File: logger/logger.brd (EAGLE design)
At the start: 100 x 80 mm, 18 parts, among them IC1 75176AD, U1 MSP430G2352IPW14

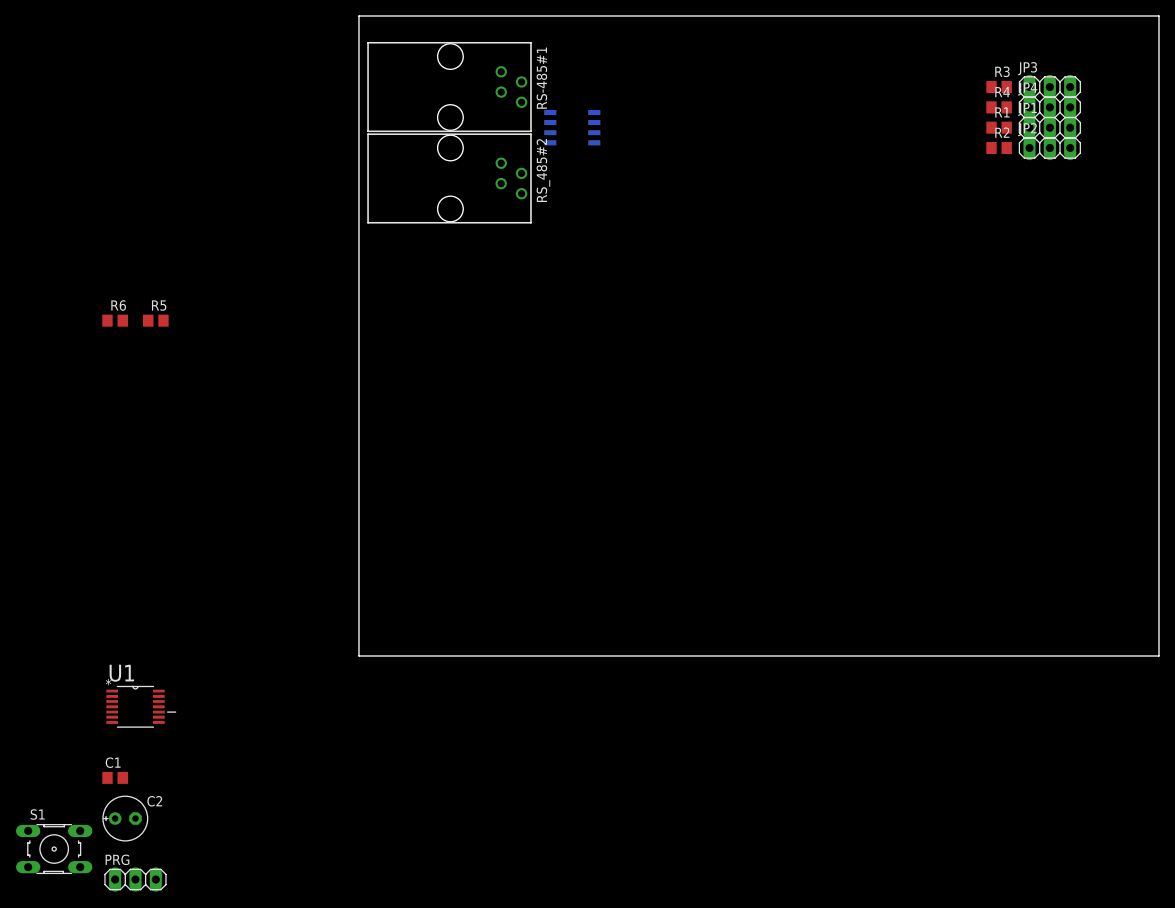
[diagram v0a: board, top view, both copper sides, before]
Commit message: Bugfixes, partially routed.
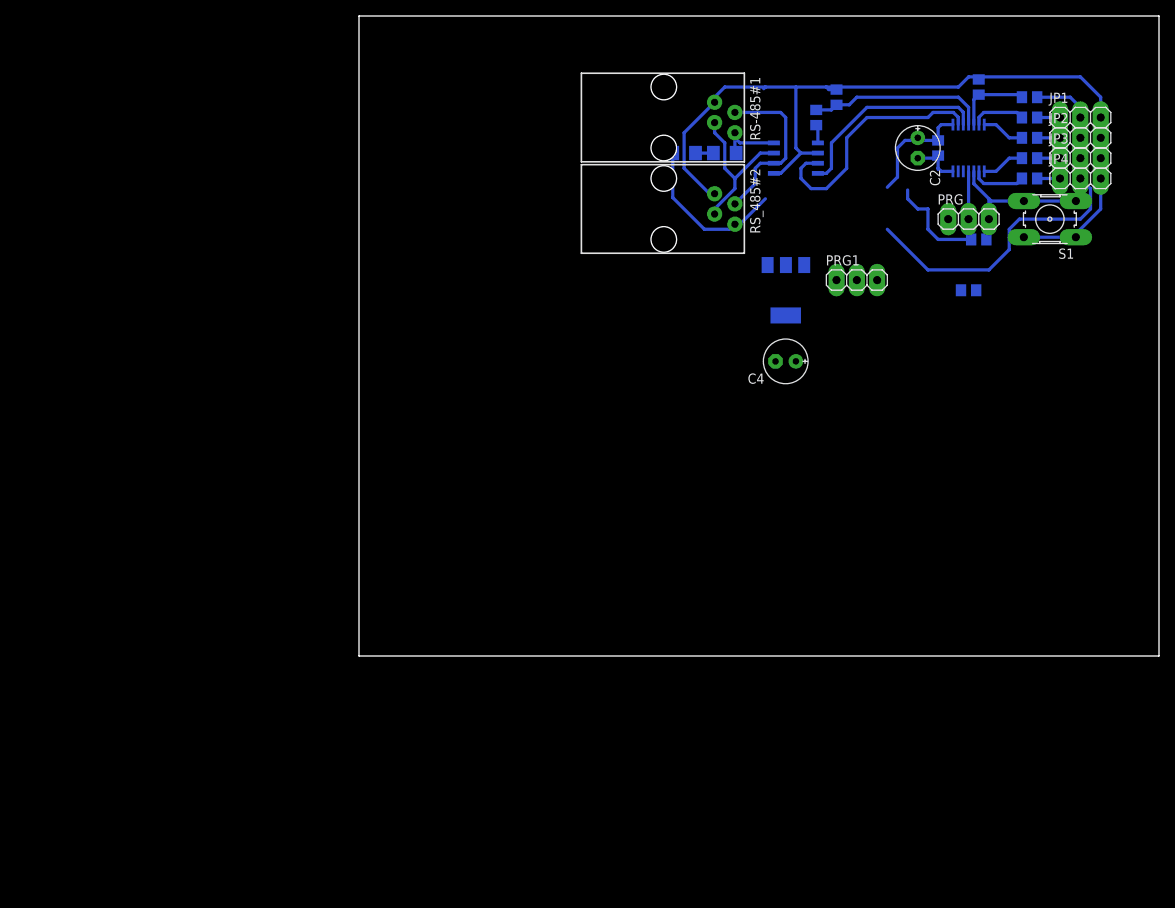
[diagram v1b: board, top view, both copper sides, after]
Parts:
- added C3: (no value), rcl:C0805
- added C4: (no value), rcl:E2,5-6E
- added IC2: REG1117, burr-brown:SOT223
- added PRG1: (no value), pinhead:1X03
- added R10, R9: (no value), rcl:R1206
- added R11, R12, R8: (no value), rcl:R0805
- moved S1 147.3 mm to (86.4, 54.6), turned to 180 degrees
- moved PRG 132.9 mm to (76.2, 54.6)
- moved C2 129.8 mm to (69.8, 63.5), turned to 270 degrees
- moved C1 129.5 mm to (72.4, 63.5), flipped to the bottom, turned to 90 degrees
- moved U1 125.4 mm to (76.2, 63.5), flipped to the bottom, turned to 270 degrees
- moved R5 112.7 mm to (83.8, 69.8), flipped to the bottom, turned to 180 degrees
- moved R6 111.8 mm to (77.5, 71.1), flipped to the bottom, turned to 270 degrees
- moved IC1 28.2 mm to (54.6, 62.2)
- moved RS-485#1 26.9 mm to (38.1, 67.3)
- moved RS_485#2 26.9 mm to (38.1, 55.9)
- moved JP3 9.67 mm to (90.2, 62.2)
- moved R3 9.67 mm to (83.8, 62.2), flipped to the bottom, turned to 180 degrees
- moved JP4 9.67 mm to (90.2, 59.7)
- moved R4 9.67 mm to (83.8, 59.7), flipped to the bottom, turned to 180 degrees
- moved JP1 4.02 mm to (90.2, 67.3)
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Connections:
- removed net N$12: IC1.1, U1.4
- new net N$17: PRG1.1, U1.13
- new net N$18: PRG1.2, U1.12
- new net N$19: R10.1, R9.2
- new net N$20: IC1.8, R9.1, RS-485#1.4
- new net N$21: IC1.1, R12.1
- new net N$22: R11.1, R12.2, U1.4
- net +3V3: now also IC2.2, R8.1
- net +5V: now also C4.+, IC2.3, JP1.2, JP2.2, JP3.2, JP4.2, R10.2; no longer IC1.5, JP1.3, JP2.3, JP3.3, JP4.3, RS-485#1.4
- net GND: now also C3.1, C4.-, IC1.5, IC2.1, JP1.3, JP2.3, JP3.3, JP4.3, PRG1.3, R11.2, S1.1, S1.2; no longer IC1.8, JP1.2, JP2.2, JP3.2, JP4.2
- net N$15: now also C3.2, R8.2, S1.3
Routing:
- net GND: track 0.00 -> 114.9 mm
- net +5V: track 0.00 -> 79.3 mm
- net N$14: track 0.00 -> 31.2 mm
- net +3V3: track 0.00 -> 27.6 mm
- net N$13: track 0.00 -> 25.3 mm
- net N$22: track 0.00 -> 22.4 mm
- net N$1: track 0.00 -> 21.5 mm
- net N$15: track 0.00 -> 20.4 mm
- net N$2: track 0.00 -> 19.7 mm
- net N$3: track 0.00 -> 9.53 mm
- net N$20: track 0.00 -> 7.74 mm
- net N$4: track 0.00 -> 6.80 mm
- net N$11: track 0.00 -> 6.80 mm
- net N$16: track 0.00 -> 5.97 mm
- net N$10: track 0.00 -> 5.40 mm
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
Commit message: Routed.
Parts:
- moved C4 17.8 mm to (52.1, 54.6), turned to 90 degrees
- moved PRG1 11.7 mm to (64.8, 58.4)
- moved C3 11.2 mm to (67.9, 53.3)
- moved IC2 9.16 mm to (58.4, 53.3), turned to 270 degrees
- moved JP2 8.98 mm to (81.3, 66.0)
- moved JP3 8.98 mm to (81.3, 63.5)
- moved JP4 8.98 mm to (81.3, 61.0)
- moved JP1 8.98 mm to (81.3, 68.6)
- moved R2 8.98 mm to (74.9, 66.0)
- moved R5 8.98 mm to (74.9, 71.1)
- moved R1 8.98 mm to (74.9, 68.6)
- moved R3 8.98 mm to (74.9, 63.5)
- moved R4 8.98 mm to (74.9, 61.0)
- moved C1 7.73 mm to (64.8, 64.8)
- moved U1 7.73 mm to (68.6, 64.8)
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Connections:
- removed net N$17: PRG1.1, U1.13
- new net N$12: PRG1.2, U1.13
- net +3V3: now also IC2.4
- net GND: now also PRG1.1; no longer PRG1.3
- net N$18: now also PRG1.3; no longer PRG1.2
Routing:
- net GND: track 114.9 -> 129.0 mm, vias 0 -> 2
- net +3V3: track 27.6 -> 40.3 mm
- net N$15: track 20.4 -> 26.9 mm
- net +5V: track 79.3 -> 83.8 mm
- net N$12: track 0.00 -> 4.47 mm
- net N$1: track 21.5 -> 17.1 mm
- net N$14: track 31.2 -> 26.8 mm
- net N$18: track 0.00 -> 3.68 mm
- net N$13: track 25.3 -> 21.8 mm
- net N$22: track 22.4 -> 19.6 mm
- net N$3: track 9.53 -> 7.26 mm
- net N$2: track 19.7 -> 17.9 mm
- net N$20: track 7.74 -> 6.05 mm
- net N$10: track 5.40 -> 4.13 mm
- net N$4: track 6.80 -> 5.53 mm
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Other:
- board size 100 x 80 mm -> 59.4 x 24.1 mm

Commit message: Final changes.
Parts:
- added JP5: (no value), pinhead:1X01
- moved R10 5.24 mm to (41.9, 57.8), turned to 270 degrees
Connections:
- net +3V3: now also JP5.1
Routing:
- net +5V: track 83.8 -> 76.3 mm
- net +3V3: track 40.3 -> 43.5 mm
- net N$19: track 2.24 -> 4.65 mm
- net GND: track 129.0 -> 131.4 mm
- added copper zone on layer 16, net GND
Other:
- board size 59.4 x 24.1 mm -> 60.6 x 26.7 mm
- board text added: "+"
- board text added: "-"
- board text added: "2013"
- board text added: "Jethro"
- board text added: "RS-485 Logger"
